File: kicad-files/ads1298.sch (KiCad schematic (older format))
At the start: 56 parts, among them J10 Conn_01x01, J11 Conn_01x01, J2 Conn_01x01, J3 Conn_01x01, J4 Conn_01x01, J5 Conn_01x01, J6 Conn_01x01, J7 Conn_01x01, J8 Conn_01x01, J9 Conn_01x01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

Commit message: more footprints
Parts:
- J10, J11, J2, J3, J4, J5, J6, J7, J8, J9: footprint (none) -> PlasticsOne:PlasticsOne_41828
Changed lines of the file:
@@
 F 0 "J2" H 11000 700 50  0000 C CNN
 F 1 "Conn_01x01" H 11000 500 50  0000 C CNN
-F 2 "" H 11000 600 50  0001 C CNN
+F 2 "PlasticsOne:PlasticsOne_41828" H 11000 600 50  0001 C CNN
 F 3 "" H 11000 600 50  0001 C CNN
 	1    11000 600
@@
 F 0 "J3" H 11000 1150 50  0000 C CNN
 F 1 "Conn_01x01" H 11000 950 50  0000 C CNN
-F 2 "" H 11000 1050 50  0001 C CNN
+F 2 "PlasticsOne:PlasticsOne_41828" H 11000 1050 50  0001 C CNN
 F 3 "" H 11000 1050 50  0001 C CNN
 	1    11000 1050
@@
 F 0 "J4" H 11000 1650 50  0000 C CNN
 F 1 "Conn_01x01" H 11000 1450 50  0000 C CNN
-F 2 "" H 11000 1550 50  0001 C CNN
+F 2 "PlasticsOne:PlasticsOne_41828" H 11000 1550 50  0001 C CNN
 F 3 "" H 11000 1550 50  0001 C CNN
 	1    11000 1550
@@
 F 0 "J5" H 11000 2100 50  0000 C CNN
 F 1 "Conn_01x01" H 11000 1900 50  0000 C CNN
-F 2 "" H 11000 2000 50  0001 C CNN
+F 2 "PlasticsOne:PlasticsOne_41828" H 11000 2000 50  0001 C CNN
 F 3 "" H 11000 2000 50  0001 C CNN
 	1    11000 2000
@@
 F 0 "J6" H 11000 2700 50  0000 C CNN
 F 1 "Conn_01x01" H 11000 2500 50  0000 C CNN
-F 2 "" H 11000 2600 50  0001 C CNN
+F 2 "PlasticsOne:PlasticsOne_41828" H 11000 2600 50  0001 C CNN
 F 3 "" H 11000 2600 50  0001 C CNN
 	1    11000 2600
@@
 F 0 "J7" H 11000 3100 50  0000 C CNN
 F 1 "Conn_01x01" H 11000 2900 50  0000 C CNN
-F 2 "" H 11000 3000 50  0001 C CNN
+F 2 "PlasticsOne:PlasticsOne_41828" H 11000 3000 50  0001 C CNN
 F 3 "" H 11000 3000 50  0001 C CNN
 	1    11000 3000
@@
 F 0 "J8" H 11000 3500 50  0000 C CNN
 F 1 "Conn_01x01" H 11000 3300 50  0000 C CNN
-F 2 "" H 11000 3400 50  0001 C CNN
+F 2 "PlasticsOne:PlasticsOne_41828" H 11000 3400 50  0001 C CNN
 F 3 "" H 11000 3400 50  0001 C CNN
 	1    11000 3400
@@
 F 0 "J9" H 11000 3900 50  0000 C CNN
 F 1 "Conn_01x01" H 11000 3700 50  0000 C CNN
-F 2 "" H 11000 3800 50  0001 C CNN
+F 2 "PlasticsOne:PlasticsOne_41828" H 11000 3800 50  0001 C CNN
 F 3 "" H 11000 3800 50  0001 C CNN
 	1    11000 3800
@@
 F 0 "J10" H 11000 4300 50  0000 C CNN
 F 1 "Conn_01x01" H 11000 4100 50  0000 C CNN
-F 2 "" H 11000 4200 50  0001 C CNN
+F 2 "PlasticsOne:PlasticsOne_41828" H 11000 4200 50  0001 C CNN
 F 3 "" H 11000 4200 50  0001 C CNN
 	1    11000 4200
@@
 F 0 "J11" H 11000 4700 50  0000 C CNN
 F 1 "Conn_01x01" H 11000 4500 50  0000 C CNN
-F 2 "" H 11000 4600 50  0001 C CNN
+F 2 "PlasticsOne:PlasticsOne_41828" H 11000 4600 50  0001 C CNN
 F 3 "" H 11000 4600 50  0001 C CNN
 	1    11000 4600

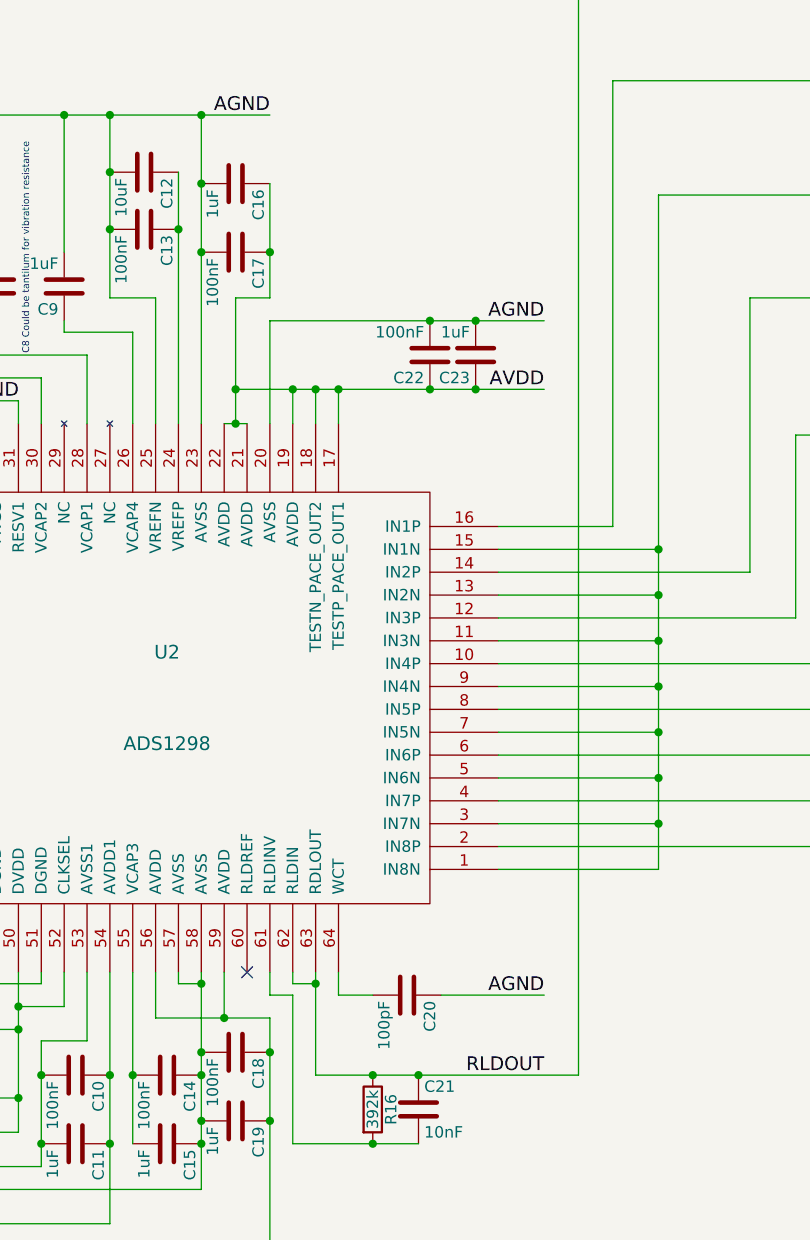
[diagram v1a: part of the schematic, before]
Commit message: wire-up power/gnd, caps to ads1298
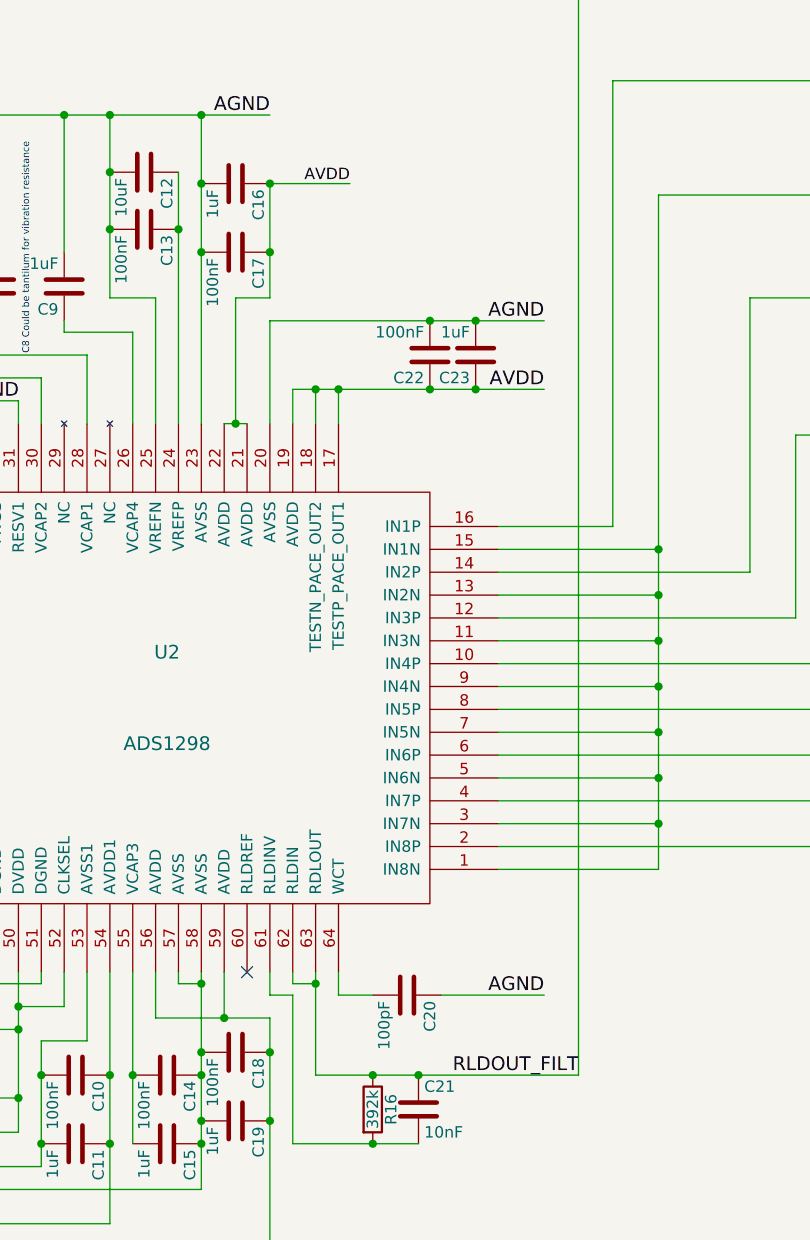
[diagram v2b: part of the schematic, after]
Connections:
- net RLDOUT: no longer C21.1, C24.1, R16.1, R17.2, U2.62 (RLDIN), U2.63 (RDLOUT)
- new net RLDOUT_FILT: C21.1, C24.1, R16.1, R17.2, U2.62 (RLDIN), U2.63 (RDLOUT)
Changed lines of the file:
@@
 Text Label 7000 5050 2    60   ~ 0
 AGND
-Text Label 7000 5400 2    60   ~ 0
-RLDOUT
+Text Label 7150 5400 2    60   ~ 0
+RLDOUT_FILT
 $Comp
 L OpenHardwareHolterMonitor-rescue:R R15
@@
 Wire Wire Line
 	5900 2550 5900 2400
-Wire Wire Line
-	5650 2400 5900 2400
 Connection ~ 6500 2400
 Wire Wire Line
 	5800 2000 5650 2000
-Wire Wire Line
-	5650 2000 5650 2400
 Wire Wire Line
 	5600 2550 5650 2550
@@
 	2100 6050 5100 6050
 Connection ~ 6700 2100
-Connection ~ 5650 2400
-Connection ~ 5900 2400
 Wire Wire Line
 	5800 1500 5800 1800
@@
 	6700 2100 7000 2100
 Wire Wire Line
-	5650 2400 5650 2550
-Wire Wire Line
 	5900 2400 6000 2400
 Wire Wire Line
@@
 Wire Wire Line
 	7500 3100 7500 3300
+Wire Wire Line
+	5650 2000 5650 2550
+Wire Wire Line
+	5800 1500 6150 1500
+Connection ~ 5800 1500
+Text Label 6150 1500 2    50   ~ 0
+AVDD
 $EndSCHEMATC

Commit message: add the first few part numbers
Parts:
- C11, C15, C16, C19, C23, C3, C5, C7, C9: manufacturer-pn (none) -> LMK107B7105KA-T
- C12: manufacturer-pn (none) -> EMK212BB7106KG-T
- C8: manufacturer-pn (none) -> GRM21BD71A226ME44L
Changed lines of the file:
@@
 F 2 "Capacitors_SMD:C_0603_HandSoldering" H 5688 1350 50  0001 C CNN
 F 3 "" H 5650 1500 50  0000 C CNN
+F 4 "LMK107B7105KA-T" H 0   0   50  0001 C CNN "manufacturer-pn"
 	1    5650 1500
 	0    1    1    0
@@
 F 2 "Capacitors_SMD:C_0603_HandSoldering" H 6738 2100 50  0001 C CNN
 F 3 "" H 6700 2250 50  0000 C CNN
+F 4 "LMK107B7105KA-T" H 0   0   50  0001 C CNN "manufacturer-pn"
 	1    6700 2250
 	-1   0    0    1
@@
 F 2 "Capacitors_SMD:C_0805_HandSoldering" H 5288 1300 50  0001 C CNN
 F 3 "" H 5250 1450 50  0000 C CNN
+F 4 "EMK212BB7106KG-T" H 0   0   50  0001 C CNN "manufacturer-pn"
 	1    5250 1450
 	0    1    1    0
@@
 F 2 "Capacitors_SMD:C_0603_HandSoldering" H 5388 5550 50  0001 C CNN
 F 3 "" H 5350 5700 50  0000 C CNN
+F 4 "LMK107B7105KA-T" H 0   0   50  0001 C CNN "manufacturer-pn"
 	1    5350 5700
 	0    1    1    0
@@
 F 2 "Capacitors_SMD:C_0603_HandSoldering" H 4938 1800 50  0001 C CNN
 F 3 "" H 4900 1950 50  0000 C CNN
+F 4 "LMK107B7105KA-T" H 0   0   50  0001 C CNN "manufacturer-pn"
 	1    4900 1950
 	-1   0    0    1
@@
 F 2 "Capacitors_SMD:C_0805_HandSoldering" H 4638 1800 50  0001 C CNN
 F 3 "" H 4600 1950 50  0000 C CNN
+F 4 " GRM21BD71A226ME44L" H 0   0   50  0001 C CNN "manufacturer-pn"
 	1    4600 1950
 	-1   0    0    1
@@
 F 2 "Capacitors_SMD:C_0603_HandSoldering" H 4338 1800 50  0001 C CNN
 F 3 "" H 4300 1950 50  0000 C CNN
+F 4 "LMK107B7105KA-T" H 0   0   50  0001 C CNN "manufacturer-pn"
 	1    4300 1950
 	-1   0    0    1
@@
 F 2 "Capacitors_SMD:C_0603_HandSoldering" H 4488 5350 50  0001 C CNN
 F 3 "" H 4450 5500 50  0000 C CNN
+F 4 "LMK107B7105KA-T" H 0   0   50  0001 C CNN "manufacturer-pn"
 	1    4450 5500
 	0    1    1    0
@@
 F 2 "Capacitors_SMD:C_0603_HandSoldering" H 4988 5550 50  0001 C CNN
 F 3 "" H 4950 5700 50  0000 C CNN
+F 4 "LMK107B7105KA-T" H 0   0   50  0001 C CNN "manufacturer-pn"
 	1    4950 5700
 	0    1    1    0
@@
 F 2 "Capacitors_SMD:C_0603_HandSoldering" H 5688 5450 50  0001 C CNN
 F 3 "" H 5650 5600 50  0000 C CNN
+F 4 "LMK107B7105KA-T" H 0   0   50  0001 C CNN "manufacturer-pn"
 	1    5650 5600
 	0    1    1    0
@@
 F 2 "Capacitors_SMD:C_0603_HandSoldering" H 3538 4500 50  0001 C CNN
 F 3 "" H 3500 4650 50  0000 C CNN
+F 4 "LMK107B7105KA-T" H 0   0   50  0001 C CNN "manufacturer-pn"
 	1    3500 4650
 	1    0    0    -1

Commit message: continue assigning part numbers for BOM
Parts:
- C10, C13, C14, C17, C18, C22, C4, C6: ManufacturerName (none) -> Yageo; manufacturer-pn (none) -> CC0603JRX7R9BB104
- C11, C15, C16, C19, C23, C3, C5, C7, C9: ManufacturerName (none) -> Taiyo Yuden
- C12: ManufacturerName (none) -> Samsung Electro-Mechanics; manufacturer-pn EMK212BB7106KG-T -> CL21B106KPQNNNE
- C20: ManufacturerName (none) -> Yageo; manufacturer-pn (none) -> CC0603JRNPO9BN101
- C21: ManufacturerName (none) -> Samsung Electro-Mechanics; manufacturer-pn (none) -> CL10B103KB8NCNC
- C24, C25, C26, C27, C28, C29, C30, C31, C32, C33: ManufacturerName (none) -> Yageo; manufacturer-pn (none) -> CC0603JRNPOYBN471
- C8: ManufacturerName (none) -> TODO:C8 tantilum? Murata Electronics; manufacturer-pn GRM21BD71A226ME44L -> GRM21BD71A226ME44L
- R17, R18, R19, R20, R21, R22, R23, R24, R25, R26: ManufacturerName (none) -> Stackpole Electronics; manufacturer-pn (none) -> ASRM2JA51K0

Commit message: fix some part typos
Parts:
- R17, R18, R19, R20, R21, R22, R23, R24, R25, R26: manufacturer-pn ASRM2JA51K0 -> ASRM2JA51K0
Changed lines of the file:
@@
 F 3 "" H 10050 1050 50  0000 C CNN
 F 4 "Stackpole Electronics" H 0   0   50  0001 C CNN "ManufacturerName"
-F 5 " ASRM2JA51K0" H 0   0   50  0001 C CNN "manufacturer-pn"
+F 5 "ASRM2JA51K0" H 0   0   50  0001 C CNN "manufacturer-pn"
 	1    10050 1050
 	0    1    1    0
@@
 F 3 "" H 10050 2000 50  0000 C CNN
 F 4 "Stackpole Electronics" H 0   0   50  0001 C CNN "ManufacturerName"
-F 5 " ASRM2JA51K0" H 0   0   50  0001 C CNN "manufacturer-pn"
+F 5 "ASRM2JA51K0" H 0   0   50  0001 C CNN "manufacturer-pn"
 	1    10050 2000
 	0    1    1    0
@@
 F 3 "" H 10050 2600 50  0000 C CNN
 F 4 "Stackpole Electronics" H 0   0   50  0001 C CNN "ManufacturerName"
-F 5 " ASRM2JA51K0" H 0   0   50  0001 C CNN "manufacturer-pn"
+F 5 "ASRM2JA51K0" H 0   0   50  0001 C CNN "manufacturer-pn"
 	1    10050 2600
 	0    1    1    0
@@
 F 3 "" H 10050 3000 50  0000 C CNN
 F 4 "Stackpole Electronics" H 0   0   50  0001 C CNN "ManufacturerName"
-F 5 " ASRM2JA51K0" H 0   0   50  0001 C CNN "manufacturer-pn"
+F 5 "ASRM2JA51K0" H 0   0   50  0001 C CNN "manufacturer-pn"
 	1    10050 3000
 	0    1    1    0
@@
 F 3 "" H 10050 3400 50  0000 C CNN
 F 4 "Stackpole Electronics" H 0   0   50  0001 C CNN "ManufacturerName"
-F 5 " ASRM2JA51K0" H 0   0   50  0001 C CNN "manufacturer-pn"
+F 5 "ASRM2JA51K0" H 0   0   50  0001 C CNN "manufacturer-pn"
 	1    10050 3400
 	0    1    1    0
@@
 F 3 "" H 10050 3800 50  0000 C CNN
 F 4 "Stackpole Electronics" H 0   0   50  0001 C CNN "ManufacturerName"
-F 5 " ASRM2JA51K0" H 0   0   50  0001 C CNN "manufacturer-pn"
+F 5 "ASRM2JA51K0" H 0   0   50  0001 C CNN "manufacturer-pn"
 	1    10050 3800
 	0    1    1    0
@@
 F 3 "" H 10050 4200 50  0000 C CNN
 F 4 "Stackpole Electronics" H 0   0   50  0001 C CNN "ManufacturerName"
-F 5 " ASRM2JA51K0" H 0   0   50  0001 C CNN "manufacturer-pn"
+F 5 "ASRM2JA51K0" H 0   0   50  0001 C CNN "manufacturer-pn"
 	1    10050 4200
 	0    1    1    0
@@
 F 3 "" H 10050 4600 50  0000 C CNN
 F 4 "Stackpole Electronics" H 0   0   50  0001 C CNN "ManufacturerName"
-F 5 " ASRM2JA51K0" H 0   0   50  0001 C CNN "manufacturer-pn"
+F 5 "ASRM2JA51K0" H 0   0   50  0001 C CNN "manufacturer-pn"
 	1    10050 4600
 	0    1    1    0
@@
 F 3 "" H 10050 1550 50  0000 C CNN
 F 4 "Stackpole Electronics" H 0   0   50  0001 C CNN "ManufacturerName"
-F 5 " ASRM2JA51K0" H 0   0   50  0001 C CNN "manufacturer-pn"
+F 5 "ASRM2JA51K0" H 0   0   50  0001 C CNN "manufacturer-pn"
 	1    10050 1550
 	0    1    1    0
@@
 F 3 "" H 10050 600 50  0000 C CNN
 F 4 "Stackpole Electronics" H 0   0   50  0001 C CNN "ManufacturerName"
-F 5 " ASRM2JA51K0" H 0   0   50  0001 C CNN "manufacturer-pn"
+F 5 "ASRM2JA51K0" H 0   0   50  0001 C CNN "manufacturer-pn"
 	1    10050 600
 	0    1    1    0

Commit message: someone set us up the BoM
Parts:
- J10, J11, J2, J3, J4, J5, J6, J7, J8, J9: ManufacturerName (none) -> PlasticsOne; manufacturer-pn (none) -> 41828
- R13: ManufacturerName (none) -> Panasonic Electronic Components; manufacturer-pn (none) -> ERA-3AEB104V
- R14, R15: ManufacturerName (none) -> Panasonic Electronic Components; manufacturer-pn (none) -> ERA-3AEB470V
- R16: ManufacturerName (none) -> TE Connectivity Passive Product; manufacturer-pn (none) -> RN73C1J392KBTD
- U2: ManufacturerName (none) -> Texas Instruments; manufacturer-pn (none) -> ADS1298IPAG
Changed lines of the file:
@@
 F 2 "Housings_QFP:LQFP-64_10x10mm_Pitch0.5mm" H 5350 3750 60  0001 C CNN
 F 3 "" H 5350 3750 60  0001 C CNN
+F 4 "Texas Instruments" H 0   0   50  0001 C CNN "ManufacturerName"
+F 5 "ADS1298IPAG" H 0   0   50  0001 C CNN "manufacturer-pn"
 	1    5350 3750
 	-1   0    0    1
@@
 F 2 "Resistors_SMD:R_0603_HandSoldering" V 6180 5550 50  0001 C CNN
 F 3 "" H 6250 5550 50  0000 C CNN
+F 4 "TE Connectivity Passive Product" H 0   0   50  0001 C CNN "ManufacturerName"
+F 5 "RN73C1J392KBTD" H 0   0   50  0001 C CNN "manufacturer-pn"
 	1    6250 5550
 	1    0    0    -1
@@
 F 2 "Resistors_SMD:R_0603_HandSoldering" V 2980 4400 50  0001 C CNN
 F 3 "" H 3050 4400 50  0000 C CNN
+F 4 "Panasonic Electronic Components" H 0   0   50  0001 C CNN "ManufacturerName"
+F 5 "ERA-3AEB470V" H 0   0   50  0001 C CNN "manufacturer-pn"
 	1    3050 4400
 	0    1    1    0
@@
 F 2 "Resistors_SMD:R_0603_HandSoldering" V 2980 4000 50  0001 C CNN
 F 3 "" H 3050 4000 50  0000 C CNN
+F 4 "Panasonic Electronic Components" H 0   0   50  0001 C CNN "ManufacturerName"
+F 5 "ERA-3AEB470V" H 0   0   50  0001 C CNN "manufacturer-pn"
 	1    3050 4000
 	0    1    1    0
@@
 F 2 "Resistors_SMD:R_0603_HandSoldering" V 2980 3800 50  0001 C CNN
 F 3 "" H 3050 3800 50  0000 C CNN
+F 4 "Panasonic Electronic Components" H 0   0   50  0001 C CNN "ManufacturerName"
+F 5 "ERA-3AEB104V" H 0   0   50  0001 C CNN "manufacturer-pn"
 	1    3050 3800
 	0    1    1    0
@@
 F 2 "PlasticsOne:PlasticsOne_41828" H 11000 600 50  0001 C CNN
 F 3 "" H 11000 600 50  0001 C CNN
+F 4 "PlasticsOne" H 0   0   50  0001 C CNN "ManufacturerName"
+F 5 "41828" H 0   0   50  0001 C CNN "manufacturer-pn"
 	1    11000 600
 	1    0    0    -1
@@
 F 2 "PlasticsOne:PlasticsOne_41828" H 11000 1050 50  0001 C CNN
 F 3 "" H 11000 1050 50  0001 C CNN
+F 4 "PlasticsOne" H 0   0   50  0001 C CNN "ManufacturerName"
+F 5 "41828" H 0   0   50  0001 C CNN "manufacturer-pn"
 	1    11000 1050
 	1    0    0    -1
@@
 F 2 "PlasticsOne:PlasticsOne_41828" H 11000 1550 50  0001 C CNN
 F 3 "" H 11000 1550 50  0001 C CNN
+F 4 "PlasticsOne" H 0   0   50  0001 C CNN "ManufacturerName"
+F 5 "41828" H 0   0   50  0001 C CNN "manufacturer-pn"
 	1    11000 1550
 	1    0    0    -1
@@
 F 2 "PlasticsOne:PlasticsOne_41828" H 11000 2000 50  0001 C CNN
 F 3 "" H 11000 2000 50  0001 C CNN
+F 4 "PlasticsOne" H 0   0   50  0001 C CNN "ManufacturerName"
+F 5 "41828" H 0   0   50  0001 C CNN "manufacturer-pn"
 	1    11000 2000
 	1    0    0    -1
@@
 F 2 "PlasticsOne:PlasticsOne_41828" H 11000 2600 50  0001 C CNN
 F 3 "" H 11000 2600 50  0001 C CNN
+F 4 "PlasticsOne" H 0   0   50  0001 C CNN "ManufacturerName"
+F 5 "41828" H 0   0   50  0001 C CNN "manufacturer-pn"
 	1    11000 2600
 	1    0    0    -1
@@
 F 2 "PlasticsOne:PlasticsOne_41828" H 11000 3000 50  0001 C CNN
 F 3 "" H 11000 3000 50  0001 C CNN
+F 4 "PlasticsOne" H 0   0   50  0001 C CNN "ManufacturerName"
+F 5 "41828" H 0   0   50  0001 C CNN "manufacturer-pn"
 	1    11000 3000
 	1    0    0    -1
@@
 F 2 "PlasticsOne:PlasticsOne_41828" H 11000 3400 50  0001 C CNN
 F 3 "" H 11000 3400 50  0001 C CNN
+F 4 "PlasticsOne" H 0   0   50  0001 C CNN "ManufacturerName"
+F 5 "41828" H 0   0   50  0001 C CNN "manufacturer-pn"
 	1    11000 3400
 	1    0    0    -1
@@
 F 2 "PlasticsOne:PlasticsOne_41828" H 11000 3800 50  0001 C CNN
 F 3 "" H 11000 3800 50  0001 C CNN
+F 4 "PlasticsOne" H 0   0   50  0001 C CNN "ManufacturerName"
+F 5 "41828" H 0   0   50  0001 C CNN "manufacturer-pn"
 	1    11000 3800
 	1    0    0    -1
@@
 F 2 "PlasticsOne:PlasticsOne_41828" H 11000 4200 50  0001 C CNN
 F 3 "" H 11000 4200 50  0001 C CNN
+F 4 "PlasticsOne" H 0   0   50  0001 C CNN "ManufacturerName"
+F 5 "41828" H 0   0   50  0001 C CNN "manufacturer-pn"
 	1    11000 4200
 	1    0    0    -1
@@
 F 2 "PlasticsOne:PlasticsOne_41828" H 11000 4600 50  0001 C CNN
 F 3 "" H 11000 4600 50  0001 C CNN
+F 4 "PlasticsOne" H 0   0   50  0001 C CNN "ManufacturerName"
+F 5 "41828" H 0   0   50  0001 C CNN "manufacturer-pn"
 	1    11000 4600
 	1    0    0    -1

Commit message: checked BoM
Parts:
- C8: ManufacturerName TODO:C8 tantilum? Murata Electronics -> Murata Electronics
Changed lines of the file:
@@
 F 3 "" H 4600 1950 50  0000 C CNN
 F 4 "GRM21BD71A226ME44L" H 0   0   50  0001 C CNN "manufacturer-pn"
-F 5 "TODO:C8 tantilum? Murata Electronics" H 0   0   50  0001 C CNN "ManufacturerName"
+F 5 "Murata Electronics" H 0   0   50  0001 C CNN "ManufacturerName"
 	1    4600 1950
 	-1   0    0    1
